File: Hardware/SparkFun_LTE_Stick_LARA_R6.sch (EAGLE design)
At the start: 75 parts, among them IC1 SN74AVC4T774PW, IC3 SN74AVC4T774PW, J1 NANO_SIM, U1 LARA-R6401, U2 AP7361C-33

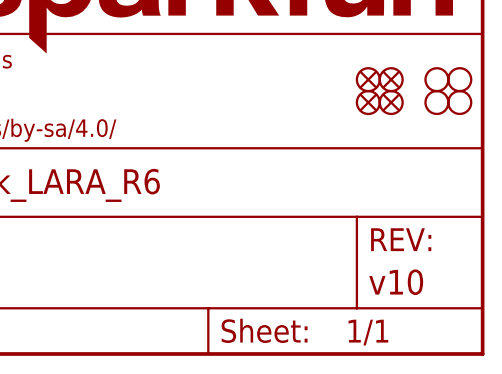
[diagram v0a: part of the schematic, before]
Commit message: v11 - Label SMA connectors in silkscreen
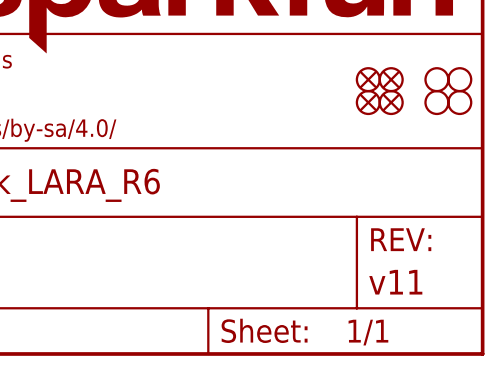
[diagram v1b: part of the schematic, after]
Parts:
- FRAME1: REV v10 -> v11
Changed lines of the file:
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@@
 <part name="FRAME1" library="SparkFun-Aesthetics" deviceset="FRAME-LEDGER" device="">
 <attribute name="DESIGNER" value="Dryw Wade"/>
-<attribute name="REV" value="v10"/>
+<attribute name="REV" value="v11"/>
 </part>
 </parts>

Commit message: Swap 100uF capacitor for new alternative
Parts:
- C9: device SparkFun-Capacitors:100UF-POLAR-25V-20%(ELEC) -> SparkFun-Capacitors:100UF-POLAR-35V-20%(ELEC)
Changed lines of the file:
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@@
 <part name="SUPPLY29" library="SparkFun-PowerSymbols" deviceset="3.3V" device=""/>
 <part name="GND2" library="SparkFun-PowerSymbols" deviceset="GND" device=""/>
-<part name="C9" library="SparkFun-Capacitors" deviceset="100UF-POLAR" device="-25V-20%(ELEC)" value="100uF"/>
+<part name="C9" library="SparkFun-Capacitors" deviceset="100UF-POLAR" device="-35V-20%(ELEC)" value="100uF"/>
 <part name="C11" library="SparkFun-Capacitors" deviceset="10UF" device="-0805-25V-10%" value="10uF"/>
 <part name="C10" library="SparkFun-Capacitors" deviceset="0.1UF" device="-0603-25V-5%" value="0.1uF"/>
